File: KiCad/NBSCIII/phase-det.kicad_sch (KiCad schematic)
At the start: 34 parts, among them Q1100 BC337-25, U1 LM324N

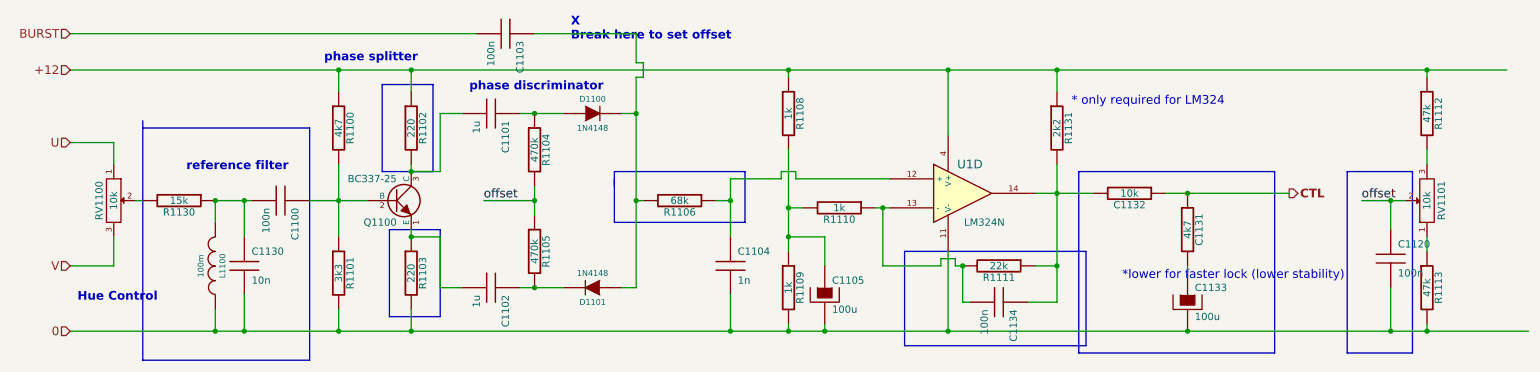
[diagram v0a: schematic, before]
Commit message: unrescue to Device:C
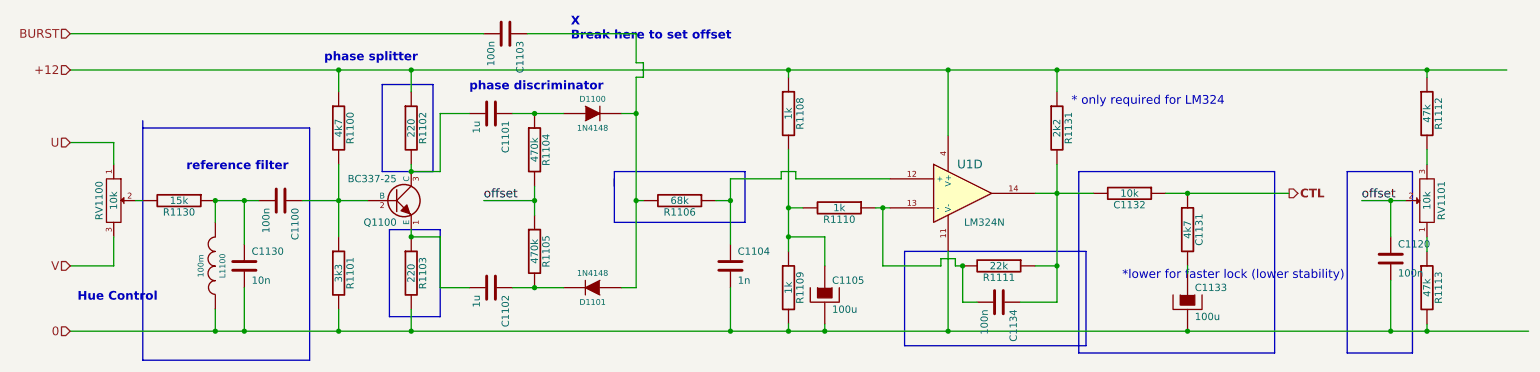
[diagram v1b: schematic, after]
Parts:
- C1100, C1101, C1102, C1103, C1104, C1120, C1130, C1134: symbol NBSCIII-rescue:C -> Device:C
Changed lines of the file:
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@@
     (stroke (width 0) (type default) (color 0 0 0 0))
   )
-  (wire (pts (xy 93.98 31.75) (xy 90.17 31.75))
+  (wire (pts (xy 90.17 31.75) (xy 95.25 31.75))
     (stroke (width 0) (type default) (color 0 0 0 0))
   )
@@
     (stroke (width 0) (type default) (color 0 0 0 0))
   )
-  (wire (pts (xy 55.88 63.5) (xy 55.88 69.85))
+  (wire (pts (xy 55.88 62.23) (xy 55.88 69.85))
+    (stroke (width 0) (type default) (color 0 0 0 0))
+  )
+  (wire (pts (xy 25.4 17.78) (xy 97.79 17.78))
     (stroke (width 0) (type default) (color 0 0 0 0))
   )
@@
     (stroke (width 0) (type default) (color 0 0 0 0))
   )
-  (wire (pts (xy 106.68 31.75) (xy 104.14 31.75))
+  (wire (pts (xy 102.87 31.75) (xy 106.68 31.75))
     (stroke (width 0) (type default) (color 0 0 0 0))
   )
@@
     (stroke (width 0) (type default) (color 0 0 0 0))
   )
-  (wire (pts (xy 106.68 62.23) (xy 104.14 62.23))
+  (wire (pts (xy 102.87 62.23) (xy 106.68 62.23))
     (stroke (width 0) (type default) (color 0 0 0 0))
   )
@@
     (stroke (width 0) (type default) (color 0 0 0 0))
   )
+  (wire (pts (xy 105.41 17.78) (xy 124.46 17.78))
+    (stroke (width 0) (type default) (color 0 0 0 0))
+  )
   (wire (pts (xy 140.97 46.99) (xy 138.43 46.99))
     (stroke (width 0) (type default) (color 0 0 0 0))
@@
     (stroke (width 0) (type default) (color 0 0 0 0))
   )
-  (wire (pts (xy 256.54 52.07) (xy 256.54 46.99))
+  (wire (pts (xy 256.54 46.99) (xy 256.54 53.34))
     (stroke (width 0) (type default) (color 0 0 0 0))
   )
@@
     (stroke (width 0) (type default) (color 0 0 0 0))
   )
-  (wire (pts (xy 124.46 17.78) (xy 106.68 17.78))
-    (stroke (width 0) (type default) (color 0 0 0 0))
-  )
   (wire (pts (xy 72.39 69.85) (xy 85.09 69.85))
     (stroke (width 0) (type default) (color 0 0 0 0))
@@
     (stroke (width 0) (type default) (color 0 0 0 0))
   )
-  (wire (pts (xy 72.39 46.99) (xy 67.31 46.99))
-    (stroke (width 0) (type default) (color 0 0 0 0))
-  )
   (wire (pts (xy 262.89 38.1) (xy 262.89 40.64))
     (stroke (width 0) (type default) (color 0 0 0 0))
@@
     (stroke (width 0) (type default) (color 0 0 0 0))
   )
-  (wire (pts (xy 182.88 64.77) (xy 181.61 64.77))
+  (wire (pts (xy 181.61 64.77) (xy 184.15 64.77))
     (stroke (width 0) (type default) (color 0 0 0 0))
   )
@@
     (stroke (width 0) (type default) (color 0 0 0 0))
   )
-  (wire (pts (xy 25.4 17.78) (xy 96.52 17.78))
-    (stroke (width 0) (type default) (color 0 0 0 0))
-  )
   (wire (pts (xy 124.46 46.99) (xy 125.73 46.99))
     (stroke (width 0) (type default) (color 0 0 0 0))
@@
     (stroke (width 0) (type default) (color 0 0 0 0))
   )
-  (wire (pts (xy 140.97 53.34) (xy 140.97 46.99))
-    (stroke (width 0) (type default) (color 0 0 0 0))
-  )
-  (wire (pts (xy 256.54 62.23) (xy 256.54 69.85))
+  (wire (pts (xy 140.97 46.99) (xy 140.97 54.61))
+    (stroke (width 0) (type default) (color 0 0 0 0))
+  )
+  (wire (pts (xy 256.54 60.96) (xy 256.54 69.85))
     (stroke (width 0) (type default) (color 0 0 0 0))
   )
@@
     (stroke (width 0) (type default) (color 0 0 0 0))
   )
-  (wire (pts (xy 55.88 53.34) (xy 55.88 46.99))
-    (stroke (width 0) (type default) (color 0 0 0 0))
-  )
   (wire (pts (xy 256.54 46.99) (xy 251.46 46.99))
     (stroke (width 0) (type default) (color 0 0 0 0))
@@
     (stroke (width 0) (type default) (color 0 0 0 0))
   )
-  (wire (pts (xy 90.17 62.23) (xy 93.98 62.23))
+  (wire (pts (xy 90.17 62.23) (xy 95.25 62.23))
     (stroke (width 0) (type default) (color 0 0 0 0))
   )
@@
     (stroke (width 0) (type default) (color 0 0 0 0))
   )
-  (wire (pts (xy 193.04 64.77) (xy 198.12 64.77))
-    (stroke (width 0) (type default) (color 0 0 0 0))
-  )
-  (wire (pts (xy 55.88 46.99) (xy 57.15 46.99))
+  (wire (pts (xy 191.77 64.77) (xy 198.12 64.77))
+    (stroke (width 0) (type default) (color 0 0 0 0))
+  )
+  (wire (pts (xy 55.88 46.99) (xy 58.42 46.99))
     (stroke (width 0) (type default) (color 0 0 0 0))
   )
@@
     (stroke (width 0) (type default) (color 0 0 0 0))
   )
+  (wire (pts (xy 55.88 46.99) (xy 55.88 54.61))
+    (stroke (width 0) (type default) (color 0 0 0 0))
+  )
   (wire (pts (xy 262.89 24.13) (xy 262.89 25.4))
     (stroke (width 0) (type default) (color 0 0 0 0))
@@
     (stroke (width 0) (type default) (color 0 0 0 0))
   )
-  (wire (pts (xy 140.97 63.5) (xy 140.97 69.85))
+  (wire (pts (xy 140.97 62.23) (xy 140.97 69.85))
+    (stroke (width 0) (type default) (color 0 0 0 0))
+  )
+  (wire (pts (xy 66.04 46.99) (xy 72.39 46.99))
     (stroke (width 0) (type default) (color 0 0 0 0))
   )
@@
     (pin "2")
   )
-  (symbol (lib_id "NBSCIII-rescue:C") (at 62.23 46.99 270) (unit 1)
+  (symbol (lib_id "Device:C") (at 62.23 46.99 270) (unit 1)
     (in_bom yes) (on_board yes)
     (property "Reference" "C1100" (id 0) (at 64.77 48.26 0)
@@
     (pin "2")
   )
-  (symbol (lib_id "NBSCIII-rescue:C") (at 99.06 31.75 270) (unit 1)
+  (symbol (lib_id "Device:C") (at 99.06 31.75 270) (unit 1)
     (in_bom yes) (on_board yes)
     (property "Reference" "C1101" (id 0) (at 101.6 33.02 0)
@@
     (pin "2")
   )
-  (symbol (lib_id "NBSCIII-rescue:C") (at 99.06 62.23 270) (unit 1)
+  (symbol (lib_id "Device:C") (at 99.06 62.23 270) (unit 1)
     (in_bom yes) (on_board yes)
     (property "Reference" "C1102" (id 0) (at 101.6 63.5 0)
@@
     (pin "2")
   )
-  (symbol (lib_id "NBSCIII-rescue:C") (at 101.6 17.78 270) (unit 1)
+  (symbol (lib_id "Device:C") (at 101.6 17.78 270) (unit 1)
     (in_bom yes) (on_board yes)
     (property "Reference" "C1103" (id 0) (at 104.14 19.05 0)
@@
     (pin "2")
   )
-  (symbol (lib_id "NBSCIII-rescue:C") (at 140.97 58.42 0) (unit 1)
+  (symbol (lib_id "Device:C") (at 140.97 58.42 0) (unit 1)
     (in_bom yes) (on_board yes)
     (property "Reference" "C1104" (id 0) (at 142.24 55.88 0)
@@
     (pin "2")
   )
-  (symbol (lib_id "NBSCIII-rescue:C") (at 55.88 58.42 0) (unit 1)
+  (symbol (lib_id "Device:C") (at 55.88 58.42 0) (unit 1)
     (in_bom yes) (on_board yes)
     (property "Reference" "C1130" (id 0) (at 57.15 55.88 0)
@@
     (pin "2")
   )
-  (symbol (lib_id "NBSCIII-rescue:C") (at 187.96 64.77 270) (unit 1)
+  (symbol (lib_id "Device:C") (at 187.96 64.77 270) (unit 1)
     (in_bom yes) (on_board yes)
     (property "Reference" "C1134" (id 0) (at 190.5 66.04 0)
@@
     (pin "2")
   )
-  (symbol (lib_id "NBSCIII-rescue:C") (at 256.54 57.15 0) (unit 1)
+  (symbol (lib_id "Device:C") (at 256.54 57.15 0) (unit 1)
     (in_bom yes) (on_board yes)
     (property "Reference" "C1120" (id 0) (at 257.81 54.61 0)

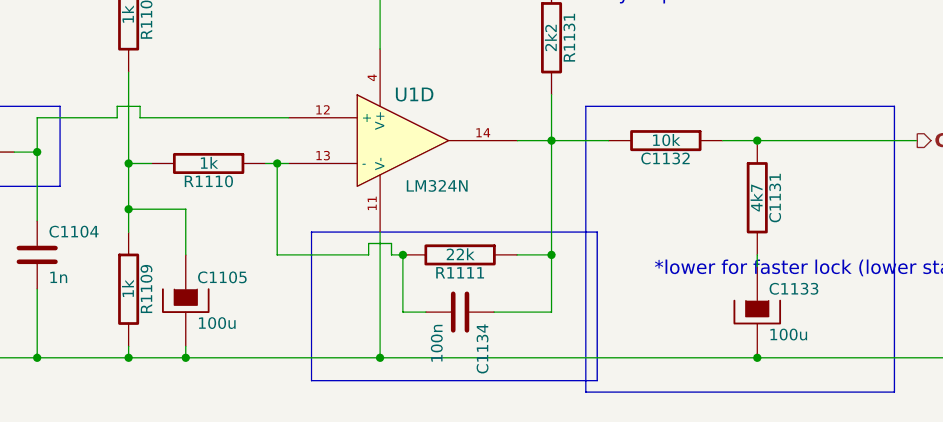
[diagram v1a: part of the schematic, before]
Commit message: unrescue to Device:C_Polarized
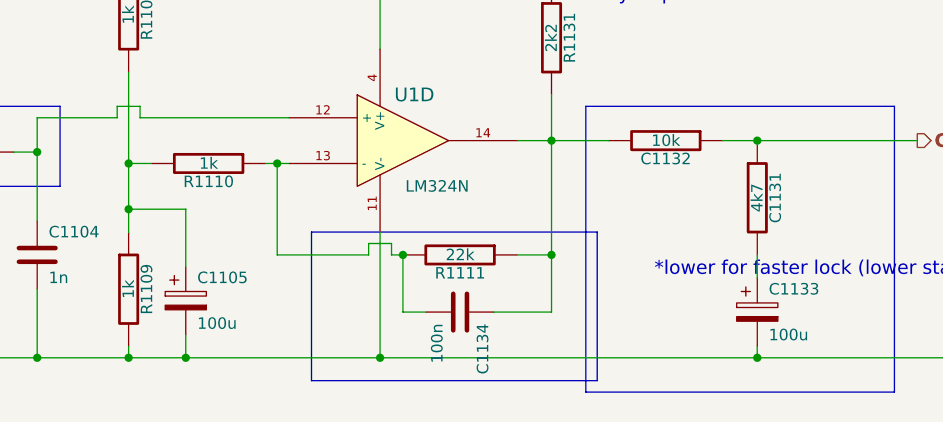
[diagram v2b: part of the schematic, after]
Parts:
- C1105, C1133: symbol NBSCIII-rescue:CP -> Device:C_Polarized
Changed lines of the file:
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@@
   (junction (at 220.98 45.72) (diameter 0) (color 0 0 0 0)
   )
+  (junction (at 262.89 69.85) (diameter 0) (color 0 0 0 0)
+  )
+  (junction (at 55.88 46.99) (diameter 0) (color 0 0 0 0)
+  )
+  (junction (at 124.46 31.75) (diameter 0) (color 0 0 0 0)
+  )
+  (junction (at 72.39 69.85) (diameter 0) (color 0 0 0 0)
+  )
+  (junction (at 262.89 24.13) (diameter 0) (color 0 0 0 0)
+  )
+  (junction (at 85.09 53.34) (diameter 0) (color 0 0 0 0)
+  )
+  (junction (at 151.13 48.26) (diameter 0) (color 0 0 0 0)
+  )
+  (junction (at 50.8 69.85) (diameter 0) (color 0 0 0 0)
+  )
+  (junction (at 179.07 24.13) (diameter 0) (color 0 0 0 0)
+  )
+  (junction (at 106.68 46.99) (diameter 0) (color 0 0 0 0)
+  )
+  (junction (at 181.61 58.42) (diameter 0) (color 0 0 0 0)
+  )
+  (junction (at 85.09 69.85) (diameter 0) (color 0 0 0 0)
+  )
+  (junction (at 106.68 62.23) (diameter 0) (color 0 0 0 0)
+  )
+  (junction (at 256.54 46.99) (diameter 0) (color 0 0 0 0)
+  )
+  (junction (at 85.09 24.13) (diameter 0) (color 0 0 0 0)
+  )
+  (junction (at 151.13 69.85) (diameter 0) (color 0 0 0 0)
+  )
+  (junction (at 72.39 24.13) (diameter 0) (color 0 0 0 0)
+  )
+  (junction (at 157.48 69.85) (diameter 0) (color 0 0 0 0)
+  )
+  (junction (at 72.39 46.99) (diameter 0) (color 0 0 0 0)
+  )
+  (junction (at 140.97 46.99) (diameter 0) (color 0 0 0 0)
+  )
+  (junction (at 151.13 53.34) (diameter 0) (color 0 0 0 0)
+  )
+  (junction (at 151.13 24.13) (diameter 0) (color 0 0 0 0)
+  )
+  (junction (at 85.09 41.91) (diameter 0) (color 0 0 0 0)
+  )
+  (junction (at 167.64 48.26) (diameter 0) (color 0 0 0 0)
+  )
+  (junction (at 198.12 45.72) (diameter 0) (color 0 0 0 0)
+  )
+  (junction (at 140.97 69.85) (diameter 0) (color 0 0 0 0)
+  )
+  (junction (at 55.88 69.85) (diameter 0) (color 0 0 0 0)
+  )
+  (junction (at 198.12 24.13) (diameter 0) (color 0 0 0 0)
+  )
+  (junction (at 50.8 46.99) (diameter 0) (color 0 0 0 0)
+  )
+  (junction (at 198.12 58.42) (diameter 0) (color 0 0 0 0)
+  )
+  (junction (at 124.46 46.99) (diameter 0) (color 0 0 0 0)
+  )
+  (junction (at 256.54 69.85) (diameter 0) (color 0 0 0 0)
+  )
+  (junction (at 106.68 31.75) (diameter 0) (color 0 0 0 0)
+  )
   (junction (at 220.98 69.85) (diameter 0) (color 0 0 0 0)
   )
-  (junction (at 262.89 69.85) (diameter 0) (color 0 0 0 0)
-  )
-  (junction (at 55.88 46.99) (diameter 0) (color 0 0 0 0)
-  )
-  (junction (at 124.46 31.75) (diameter 0) (color 0 0 0 0)
-  )
-  (junction (at 72.39 69.85) (diameter 0) (color 0 0 0 0)
-  )
-  (junction (at 262.89 24.13) (diameter 0) (color 0 0 0 0)
-  )
-  (junction (at 85.09 53.34) (diameter 0) (color 0 0 0 0)
-  )
-  (junction (at 151.13 48.26) (diameter 0) (color 0 0 0 0)
-  )
-  (junction (at 50.8 69.85) (diameter 0) (color 0 0 0 0)
-  )
-  (junction (at 179.07 24.13) (diameter 0) (color 0 0 0 0)
-  )
-  (junction (at 106.68 46.99) (diameter 0) (color 0 0 0 0)
-  )
-  (junction (at 181.61 58.42) (diameter 0) (color 0 0 0 0)
-  )
-  (junction (at 85.09 69.85) (diameter 0) (color 0 0 0 0)
-  )
-  (junction (at 106.68 62.23) (diameter 0) (color 0 0 0 0)
-  )
-  (junction (at 256.54 46.99) (diameter 0) (color 0 0 0 0)
-  )
-  (junction (at 85.09 24.13) (diameter 0) (color 0 0 0 0)
-  )
-  (junction (at 151.13 69.85) (diameter 0) (color 0 0 0 0)
-  )
-  (junction (at 72.39 24.13) (diameter 0) (color 0 0 0 0)
-  )
-  (junction (at 157.48 69.85) (diameter 0) (color 0 0 0 0)
-  )
-  (junction (at 72.39 46.99) (diameter 0) (color 0 0 0 0)
-  )
-  (junction (at 140.97 46.99) (diameter 0) (color 0 0 0 0)
-  )
-  (junction (at 151.13 53.34) (diameter 0) (color 0 0 0 0)
-  )
-  (junction (at 151.13 24.13) (diameter 0) (color 0 0 0 0)
-  )
-  (junction (at 85.09 41.91) (diameter 0) (color 0 0 0 0)
-  )
-  (junction (at 167.64 48.26) (diameter 0) (color 0 0 0 0)
-  )
-  (junction (at 198.12 45.72) (diameter 0) (color 0 0 0 0)
-  )
-  (junction (at 140.97 69.85) (diameter 0) (color 0 0 0 0)
-  )
-  (junction (at 55.88 69.85) (diameter 0) (color 0 0 0 0)
-  )
-  (junction (at 198.12 24.13) (diameter 0) (color 0 0 0 0)
-  )
-  (junction (at 50.8 46.99) (diameter 0) (color 0 0 0 0)
-  )
-  (junction (at 198.12 58.42) (diameter 0) (color 0 0 0 0)
-  )
-  (junction (at 124.46 46.99) (diameter 0) (color 0 0 0 0)
-  )
-  (junction (at 256.54 69.85) (diameter 0) (color 0 0 0 0)
-  )
-  (junction (at 106.68 31.75) (diameter 0) (color 0 0 0 0)
-  )
   (junction (at 179.07 69.85) (diameter 0) (color 0 0 0 0)
   )
+  (wire (pts (xy 220.98 69.85) (xy 256.54 69.85))
+    (stroke (width 0) (type default) (color 0 0 0 0))
+  )
   (wire (pts (xy 151.13 48.26) (xy 151.13 53.34))
     (stroke (width 0) (type default) (color 0 0 0 0))
@@
     (stroke (width 0) (type default) (color 0 0 0 0))
   )
+  (wire (pts (xy 157.48 53.34) (xy 157.48 59.69))
+    (stroke (width 0) (type default) (color 0 0 0 0))
+  )
   (wire (pts (xy 55.88 62.23) (xy 55.88 69.85))
     (stroke (width 0) (type default) (color 0 0 0 0))
@@
     (stroke (width 0) (type default) (color 0 0 0 0))
   )
-  (wire (pts (xy 220.98 59.69) (xy 220.98 58.42))
-    (stroke (width 0) (type default) (color 0 0 0 0))
-  )
   (polyline (pts (xy 203.2 55.88) (xy 171.45 55.88))
     (stroke (width 0) (type default) (color 0 0 0 0))
@@
     (stroke (width 0) (type default) (color 0 0 0 0))
   )
+  (wire (pts (xy 124.46 46.99) (xy 125.73 46.99))
+    (stroke (width 0) (type default) (color 0 0 0 0))
+  )
+  (wire (pts (xy 125.73 25.4) (xy 125.73 22.86))
+    (stroke (width 0) (type default) (color 0 0 0 0))
+  )
+  (wire (pts (xy 198.12 64.77) (xy 198.12 58.42))
+    (stroke (width 0) (type default) (color 0 0 0 0))
+  )
+  (wire (pts (xy 33.02 53.34) (xy 33.02 58.42))
+    (stroke (width 0) (type default) (color 0 0 0 0))
+  )
   (wire (pts (xy 179.07 69.85) (xy 220.98 69.85))
     (stroke (width 0) (type default) (color 0 0 0 0))
   )
-  (wire (pts (xy 157.48 58.42) (xy 157.48 53.34))
-    (stroke (width 0) (type default) (color 0 0 0 0))
-  )
-  (wire (pts (xy 124.46 46.99) (xy 125.73 46.99))
-    (stroke (width 0) (type default) (color 0 0 0 0))
-  )
-  (wire (pts (xy 125.73 25.4) (xy 125.73 22.86))
-    (stroke (width 0) (type default) (color 0 0 0 0))
-  )
-  (wire (pts (xy 198.12 64.77) (xy 198.12 58.42))
-    (stroke (width 0) (type default) (color 0 0 0 0))
-  )
-  (wire (pts (xy 33.02 53.34) (xy 33.02 58.42))
-    (stroke (width 0) (type default) (color 0 0 0 0))
-  )
-  (wire (pts (xy 220.98 69.85) (xy 256.54 69.85))
-    (stroke (width 0) (type default) (color 0 0 0 0))
-  )
   (wire (pts (xy 85.09 52.07) (xy 85.09 53.34))
     (stroke (width 0) (type default) (color 0 0 0 0))
@@
     (stroke (width 0) (type default) (color 0 0 0 0))
   )
-  (wire (pts (xy 157.48 68.58) (xy 157.48 69.85))
+  (wire (pts (xy 157.48 67.31) (xy 157.48 69.85))
     (stroke (width 0) (type default) (color 0 0 0 0))
   )
@@
     (stroke (width 0) (type default) (color 0 0 0 0))
   )
+  (wire (pts (xy 220.98 58.42) (xy 220.98 60.96))
+    (stroke (width 0) (type default) (color 0 0 0 0))
+  )
   (wire (pts (xy 85.09 41.91) (xy 85.09 40.64))
+    (stroke (width 0) (type default) (color 0 0 0 0))
+  )
+  (wire (pts (xy 220.98 68.58) (xy 220.98 69.85))
     (stroke (width 0) (type default) (color 0 0 0 0))
   )
@@
     (pin "2")
   )
-  (symbol (lib_id "NBSCIII-rescue:CP") (at 157.48 63.5 0) (unit 1)
+  (symbol (lib_id "Device:C_Polarized") (at 157.48 63.5 0) (unit 1)
     (in_bom yes) (on_board yes)
     (property "Reference" "C1105" (id 0) (at 158.75 60.96 0)
@@
     (pin "2")
   )
-  (symbol (lib_id "NBSCIII-rescue:CP") (at 220.98 64.77 0) (unit 1)
+  (symbol (lib_id "Device:C_Polarized") (at 220.98 64.77 0) (unit 1)
     (in_bom yes) (on_board yes)
     (property "Reference" "C1133" (id 0) (at 222.25 62.23 0)

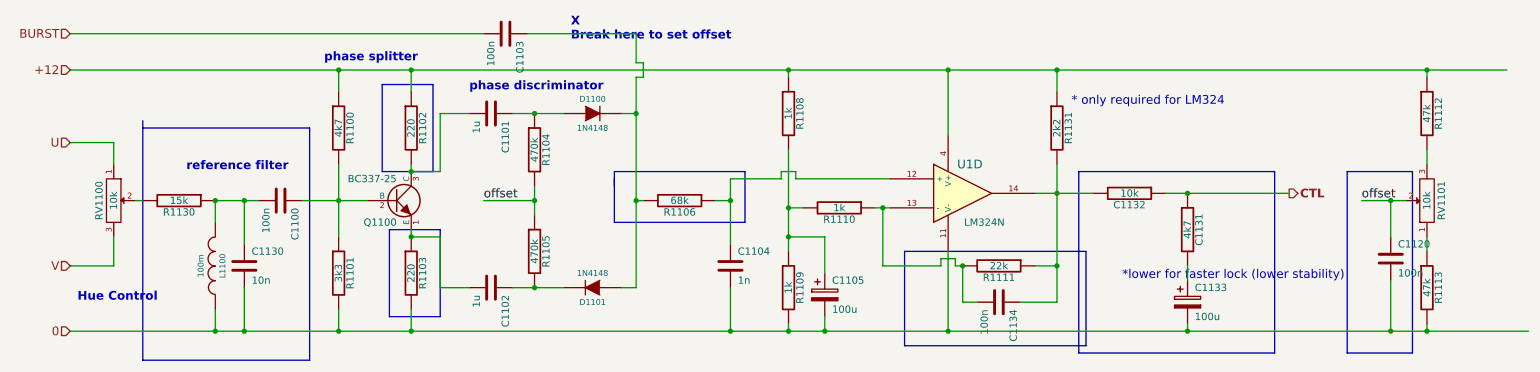
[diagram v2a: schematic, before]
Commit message: unrescue Device:R
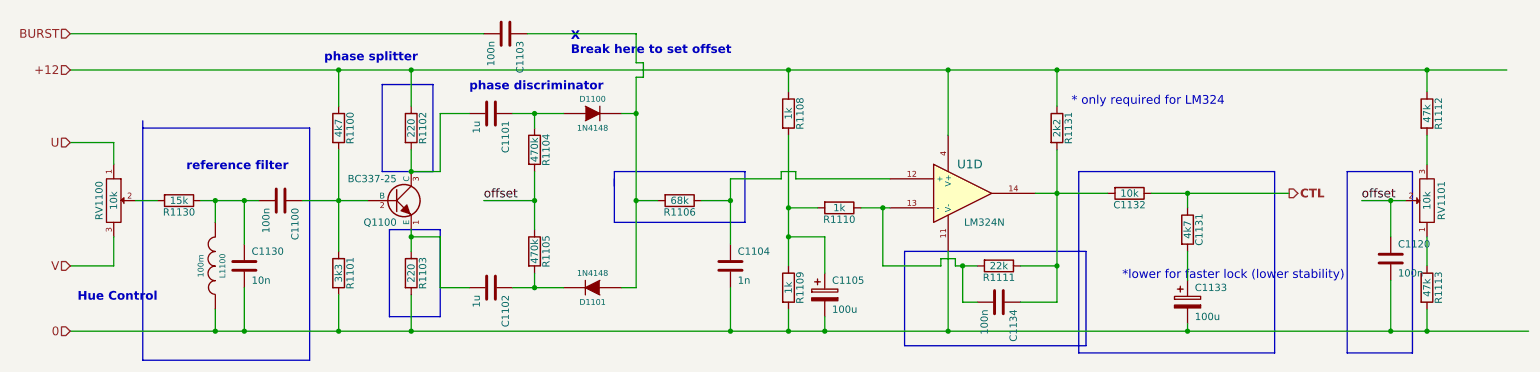
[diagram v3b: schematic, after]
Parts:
- C1131, C1132, R1100, R1101, R1102, R1103, R1104, R1105, R1106, R1108, R1109, R1110, R1111, R1112, R1113, R1130, R1131: symbol NBSCIII-rescue:R -> Device:R
